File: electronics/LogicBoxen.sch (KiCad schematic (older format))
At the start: 60 parts, among them P1 Input, P2 Out, P3 Batteria, SW1 SW_PUSH, SW2 SW_PUSH, U1 4015, U2 4011, U3 4015, U4 4015, U5 7805

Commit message: Removed excess LEDs, updated library cache
Four LEDs should be enough for the incoming signals. This has the
advantage of using a 4015 less.
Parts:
- removed D10, D11, D13, D15, D4, D6, D7, D8: LED_rosso, LEDs:LED-5MM, symbol LED
- removed P1: Input, Pin_Headers:Pin_Header_Straight_1x02, symbol CONN_2
- removed P2: Out, Pin_Headers:Pin_Header_Straight_1x02, symbol CONN_2
- removed P3: Batteria, Pin_Headers:Pin_Header_Straight_1x02, symbol CONN_2
- removed Q? (x2): 2n222, ~, symbol NPN
- removed R10, R11, R12, R14, R17, R6, R7, R8: 220, Resistors_Universal:Resistor_SMD+THTuniversal_0805to1206_RM10_HandSoldering, symbol R
- removed R? (x2): 10k, ~, symbol R
- removed unit 1 of U1
- removed unit 2 of U3
- added P1: Input, symbol CONN_01X02
- added P2: Output, symbol CONN_01X02
- added P3: Power, symbol CONN_01X02
- renumbered D19 to D10, D18 to D11, D20 to D12, D21 to D13, D9 to D4, D12 to D6, D14 to D7, D17 to D8, D16 to D9, R18 to R10, R21 to R11, R16 to R12, R20 to R13, R22 to R14, R23 to R15, R9 to R6, R13 to R7, R15 to R8, R19 to R9, U4 to U1, U5 to U4
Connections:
- wire segments 182 -> 106
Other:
- moved on the sheet: C1, C2, D1, D10, D12, D13, D2, D3, D4, D8, R1, R11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

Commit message: Update schematics and board to latest version
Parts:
- removed C1, C2: CP, Capacitors_Elko_ThroughHole:Elko_vert_11.2x6.3mm_RM2.5, symbol CP
- removed D1, D10, D11, D12, D2, D3, D6, D7, D8, D9: LED_rosso, LEDs:LED-5MM, symbol LED
- removed D13, D4, D5: LED_verde, LEDs:LED-5MM, symbol LED
- removed P3: Power, symbol CONN_01X02
- removed SW1, SW2: SW_PUSH, Buttons_Switches_ThroughHole:SW_PUSH_SMALL, symbol SW_PUSH
- removed U2: 4011, symbol 4011
- removed U4: 7805, Housings_SOIC:SOIC-16_7.5x10.3mm_Pitch1.27mm, symbol 7805
- added C1: C, Capacitors_SMD:C_0402, symbol C
- added K1: Power, Socket_Strips:Socket_Strip_Angled_1x03, symbol CONN_3
- added P3, P4: CONN_01X05, Socket_Strips:Socket_Strip_Angled_1x05, symbol CONN_01X05
- added P5: CONN_01X06, Socket_Strips:Socket_Strip_Angled_1x06, symbol CONN_01X06
- added Q1: Q_NMOS_DGS, Housings_SOT-23_SOT-143_TSOT-6:SOT-23_Handsoldering, symbol Q_NMOS_DGS
- added R16: R, Resistors_SMD:R_0402, symbol R
- added R18, R19, R20, R21: 10k, Resistors_SMD:R_0402, symbol R
- added R22: 0R, Resistors_SMD:R_0402, symbol R
- added SW1: DIPS_04, Sockets_DIP:DIP-8__300, symbol DIPS_04
- added U2, U4: 4050, Housings_SSOP:TSSOP-16_4.4x5mm_Pitch0.65mm, symbol 4050
- added unit 2 of U3
- added U6: 4051, Housings_SSOP:TSSOP-16_4.4x5mm_Pitch0.65mm, symbol 4051
- P1, P2: footprint (none) -> Socket_Strips:Socket_Strip_Angled_1x02
- R1, R10, R11, R12, R13, R14, R15, R2, R3, R4, R5, R6, R7, R8, R9: footprint Resistors_Universal:Resistor_SMD+THTuniversal_0805to1206_RM10_HandSoldering -> Resistors_SMD:R_0402; symbol R -> R-RESCUE-LogicBoxen
- U1: footprint (none) -> Housings_SSOP:TSSOP-16_4.4x5mm_Pitch0.65mm
- U1: renamed from U3; footprint (none) -> Housings_SSOP:TSSOP-16_4.4x5mm_Pitch0.65mm
- U3: renamed from U1; footprint (none) -> Housings_SSOP:TSSOP-16_4.4x5mm_Pitch0.65mm
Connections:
- net GND: now also K1.1 (P1), P3.5 (P5), P4.5 (P5), P5.6 (P6), R16.1, R18.2, R19.2, R20.2, R21.2, U2.8 (VSS), U2.8 (VSS), U2.8 (VSS), U2.8 (VSS), U2.8 (VSS), U2.8 (VSS), U4.8 (VSS), U4.8 (VSS), U4.8 (VSS), U4.8 (VSS), U4.8 (VSS), U4.8 (VSS), U6.1 (X4), U6.2 (X6), U6.4 (X7), U6.5 (X5), U6.6 (Inh), U6.8 (VSS), U6.9 (C); no longer R1.2, R10.2, R11.2, R13.2, R14.2, R15.2, R2.2, R3.2, R4.2, R5.2, R7.2, R8.2, R9.2
- net VCC: now also C1.1, K1.3 (P3), Q1.1 (D), SW1.1, SW1.2, SW1.3, SW1.4, U2.1 (VCC), U2.1 (VCC), U2.1 (VCC), U2.1 (VCC), U2.1 (VCC), U2.1 (VCC), U4.1 (VCC), U4.1 (VCC), U4.1 (VCC), U4.1 (VCC), U4.1 (VCC), U4.1 (VCC), U6.16 (VDD), U6.7 (VEE)
- net Vdd: now also U3.16 (Vdd)
- net Vss: now also U3.8 (Vss)
- net clock: now also U1.1 (CP), U3.9 (CP), K1.2 (PM); no longer U1.9 (CP), U3.1 (CP)
- net in_a: now also U4.14, U6.11 (A)
- net in_b: now also U1.2 (Q4), U4.5, U6.10 (B); no longer U1.10 (Q4)
- net out: now also U3.7 (D), Q1.2 (G), R22.1, U6.3 (X); no longer U3.15 (D)
- net reset: now also U1.14 (MR), U3.6 (MR), C1.2, R16.2; no longer U1.6 (MR), U3.14 (MR)
- net at R1.1: now also U4.6
- net at U1.5 (Q1): now also U4.7
- net at R2.1: now also U4.10
- net at U1.4 (Q2): now also U4.9
- net at R3.1: now also U4.12
- net at U1.3 (Q3): now also U4.11
- net at R9.1: now also U2.12
- net at R11.1: now also U2.15
- net at R14.1: now also U4.2
- net at R15.1: now also U4.4
- net at P1.1 (P1), R12.1: now also U1.15 (D); no longer U1.7 (D)
- net at R4.1: now also U4.15
- net at R5.1: now also Q1.3 (S), R22.2
- net at R7.1: now also U2.2
- net at R8.1: now also U2.4
- net at R10.1: now also U2.6
- net at R13.1: now also P2.2 (P2), U2.10
- new net: P3.1 (P1), R1.2
- new net: P3.2 (P2), R2.2
- new net: P3.3 (P3), R3.2
- new net: P4.1 (P1), R9.2
- new net: P4.2 (P2), R11.2
- new net: P4.3 (P3), R14.2
- new net: P4.4 (P4), R15.2
- new net: P5.2 (P2), R7.2
- new net: P5.3 (P3), R8.2
- new net: P5.4 (P4), R10.2
- new net: P5.5 (P5), R13.2
- new net: U1.11 (Q3), U4.3
- new net: U1.12 (Q2), U2.14
- new net: U1.13 (Q1), U2.11
- new net: U2.9, U3.10 (Q4)
- new net: U2.7, U3.3 (Q3)
- new net: U2.5, U3.4 (Q2)
- new net: U2.3, U3.5 (Q1)
- new net: P3.4 (P4), R4.2
- new net X0: R18.1, SW1.7, U6.13 (X0)
- new net X1: R19.1, SW1.6, U6.14 (X1)
- new net X2: R20.1, SW1.5, U6.15 (X2)
- new net X3: R21.1, SW1.8, U6.12 (X3)
- new net led_main: P5.1 (P1), R5.2
- no-connect marks 0 -> 7
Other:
- note added: "Input stage A"
- note added: "Input stage B"
- note added: "Output stage"
- note added: "Populate R22 or Q1"
- note added: "Power supply, clock\nand reset generator"
- note removed: "Linea di destra"
- note removed: "Linea di sinistra"
- moved on the sheet: P1, P2, R1, R10, R11, R12, R13, R14, R15, R2, R3, R4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

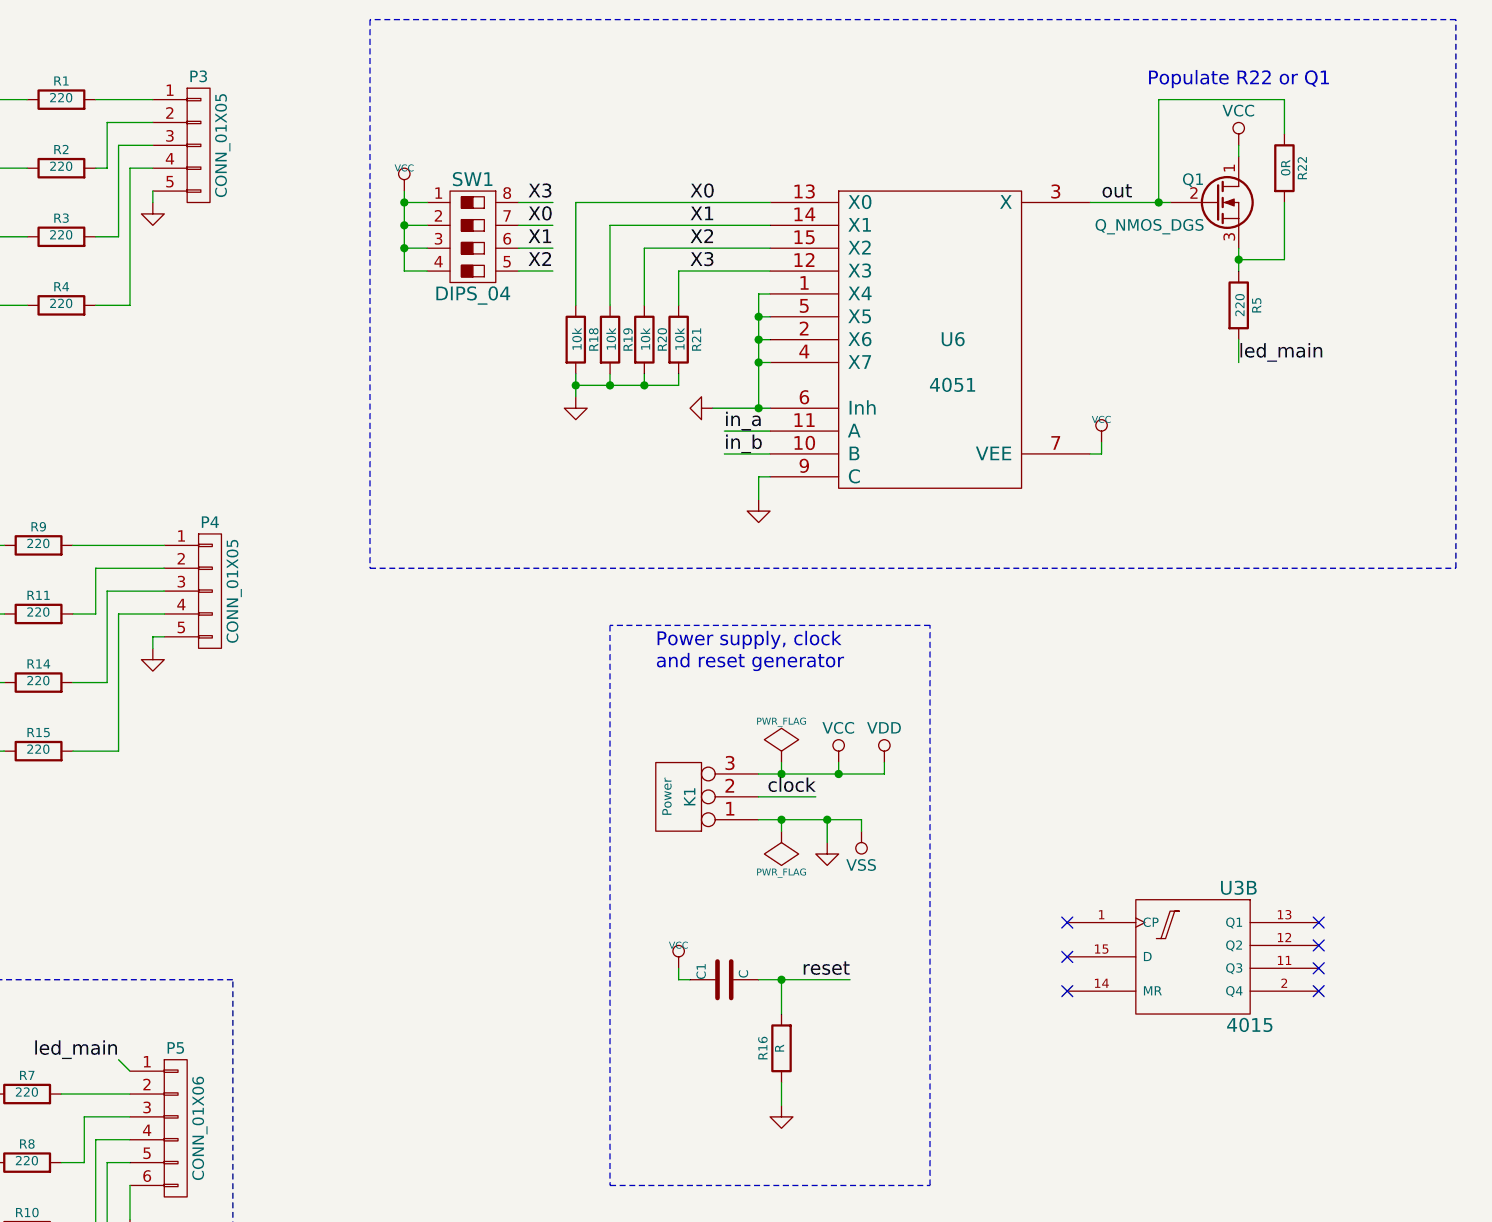
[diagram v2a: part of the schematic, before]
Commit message: Minor changes to board.
* Change refs of components to all match Px
* Add solder jumpers to avoid populating the DIP switch.
* General board track optimization.
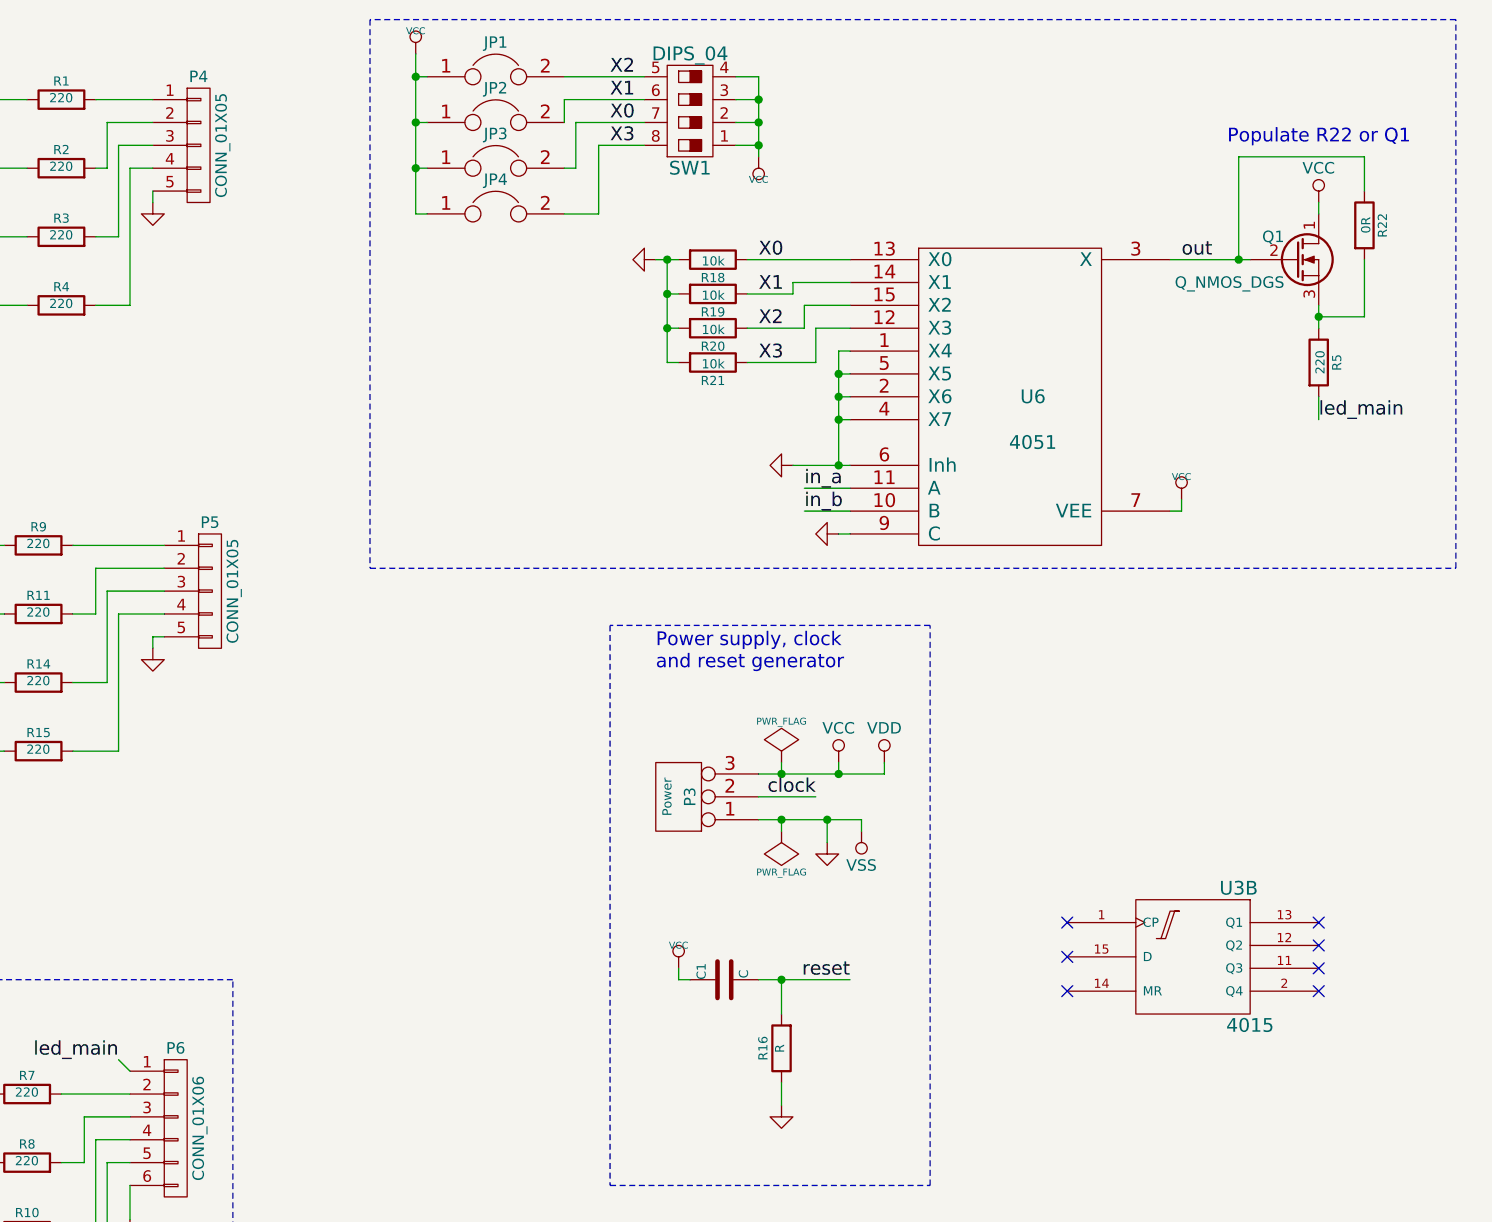
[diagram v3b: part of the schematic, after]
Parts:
- added JP1, JP2, JP3, JP4: JUMPER, Resistors_SMD:R_0805_HandSoldering, symbol JUMPER
- renumbered K1 to P3, P3 to P4, P4 to P5, P5 to P6
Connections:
- net VCC: now also JP1.1, JP2.1, JP3.1, JP4.1
- net X0: now also JP3.2
- net X1: now also JP2.2
- net X2: now also JP1.2
- net X3: now also JP4.2
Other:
- moved on the sheet: Q1, R18, R19, R20, R21, R22, R5, SW1, U6
